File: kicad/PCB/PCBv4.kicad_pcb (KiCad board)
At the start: 2 copper layers, 80 x 55 mm, 53 parts, among them J1 JST_2mm, J2 JST_2mm, J3 3.5mm, J5 Ventilador, J6 48V IN, J7 3.5mm, J9 Selector_TC4420, Q1 IRL520N, SW1 SW_DIP_x03, U1 XIAO-RP2350-DIP, U2 AP2112K-3.3, U3 TB6612FNG, U4 TC4420

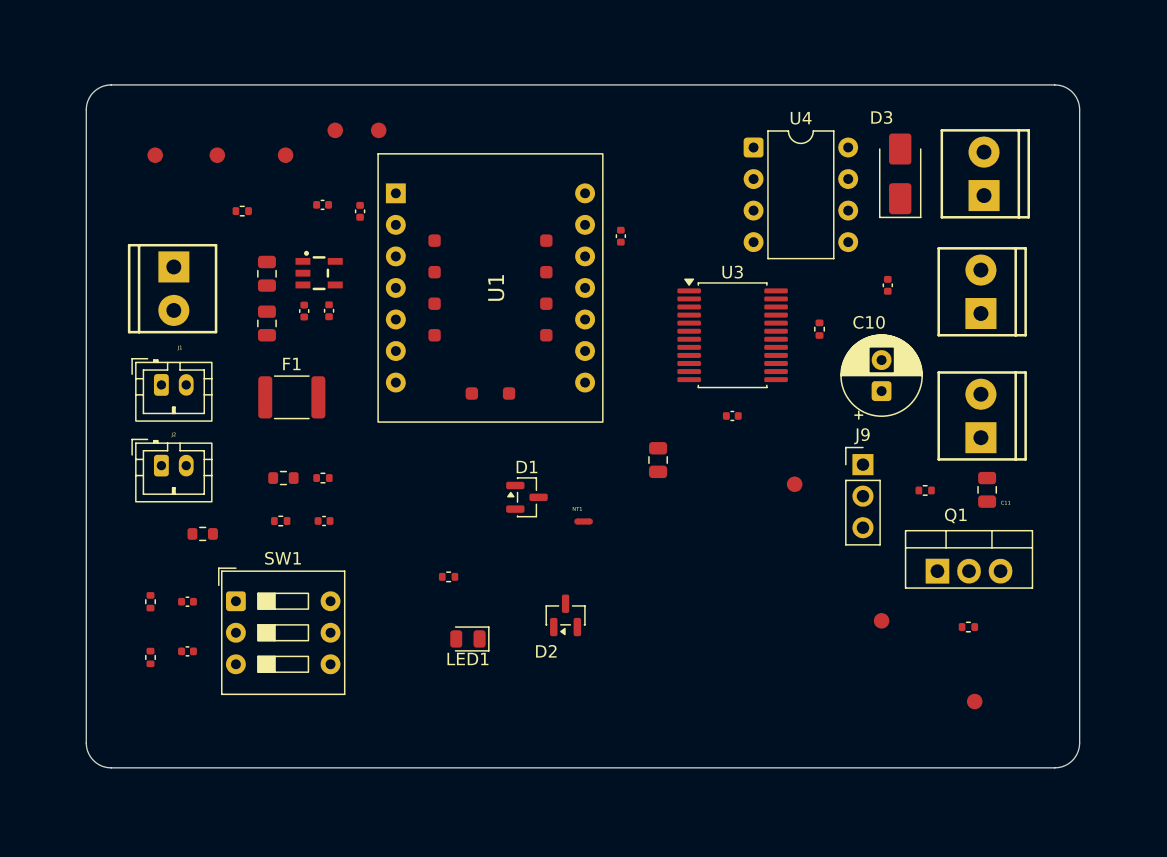
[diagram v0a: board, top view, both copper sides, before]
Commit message: chore: version 1.1.2 - Agregados planos de cobre y organizacion de archivos
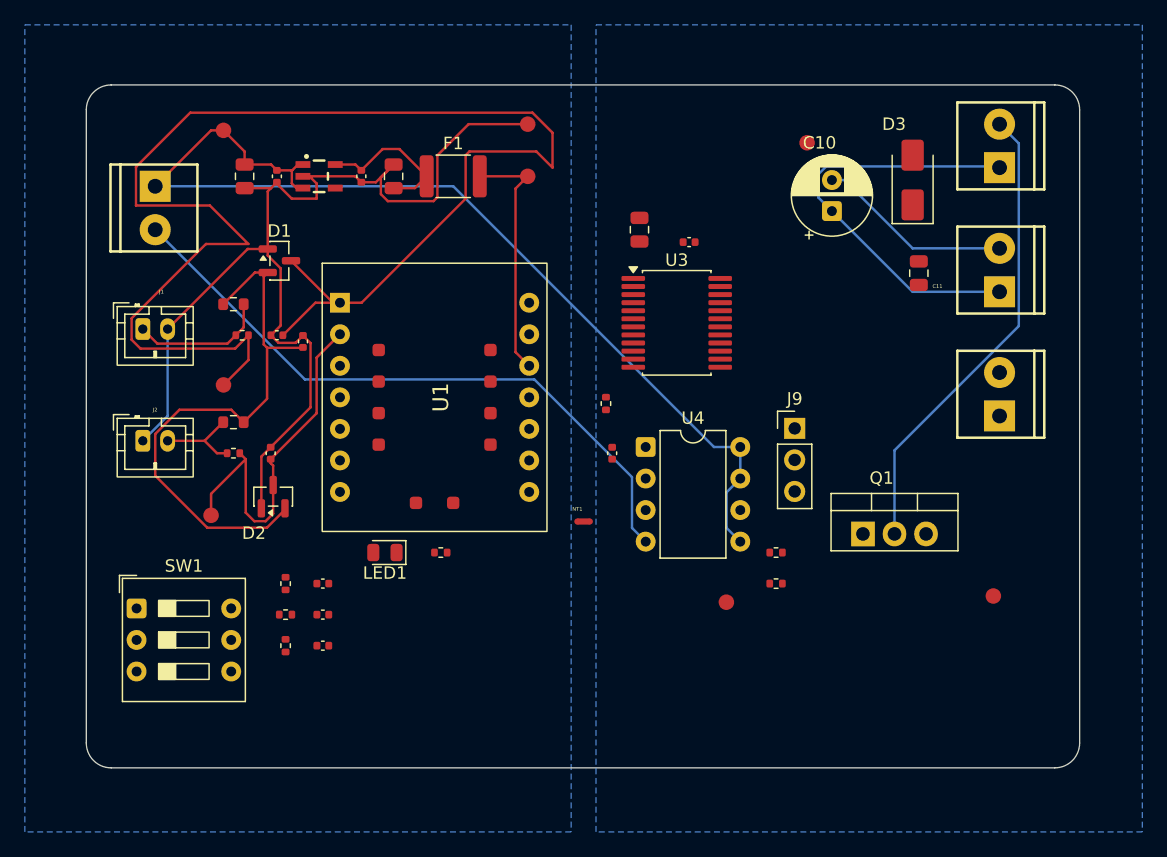
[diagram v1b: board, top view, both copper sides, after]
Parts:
- moved TP7 33.8 mm to (120.0, 104.5)
- moved TP1 30.0 mm to (145.5, 77.2)
- moved D1 27.6 mm to (125.5, 84.0)
- moved TP3 27.5 mm to (168.0, 74.5)
- moved C9 27.0 mm to (127.4, 90.5)
- moved C15 26.0 mm to (152.3, 99.5)
- moved U4 25.6 mm to (155.0, 99.0)
- moved D2 25.4 mm to (125.0, 103.0)
- moved TP6 22.4 mm to (121.0, 94.0)
- moved F1 22.0 mm to (139.5, 77.2)
- moved C6 20.8 mm to (124.8, 99.5)
- moved TP5 19.7 mm to (145.5, 73.0)
- moved R4 19.5 mm to (121.8, 99.5)
- moved C7 18.6 mm to (154.5, 81.5)
- moved C11 18.3 mm to (177.0, 85.0)
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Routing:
- net /NET_TEMP_INT_FILT: track 0.00 -> 116.6 mm
- net /AGND: track 0.00 -> 88.8 mm
- net /+5V: track 0.00 -> 82.4 mm
- net /PGND: track 0.00 -> 68.1 mm
- net /+3V3: track 0.00 -> 65.2 mm
- net /NET_FAN_HS: track 0.00 -> 37.8 mm
- net /+48V: track 0.00 -> 34.5 mm
- net /NET_TEMP_EXT_FILT: track 0.00 -> 30.3 mm
- net /NET_3V3_LDO: track 0.00 -> 12.2 mm
- net /NET_TEMP_INT_DIV: track 0.00 -> 11.0 mm
- net /NET_TEMP_EXT_DIV: track 0.00 -> 7.33 mm
- added copper zone on B.Cu, net /AGND
- added copper zone on B.Cu, net /PGND
